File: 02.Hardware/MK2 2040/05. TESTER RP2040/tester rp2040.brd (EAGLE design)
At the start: 135 x 56 mm, 59 parts, among them IC1 MAX4634EUB+T, J1 302-S201, Q1 PJA3416AE_R1_00001, Q2 2N7002PW, Q3 2N7002PW, Q4 RQ3G110ATTB, Q5 PJA3416AE_R1_00001, Q6 2N7002PW, Q7 RQ3G110ATTB, Q8 PJA3416AE_R1_00001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

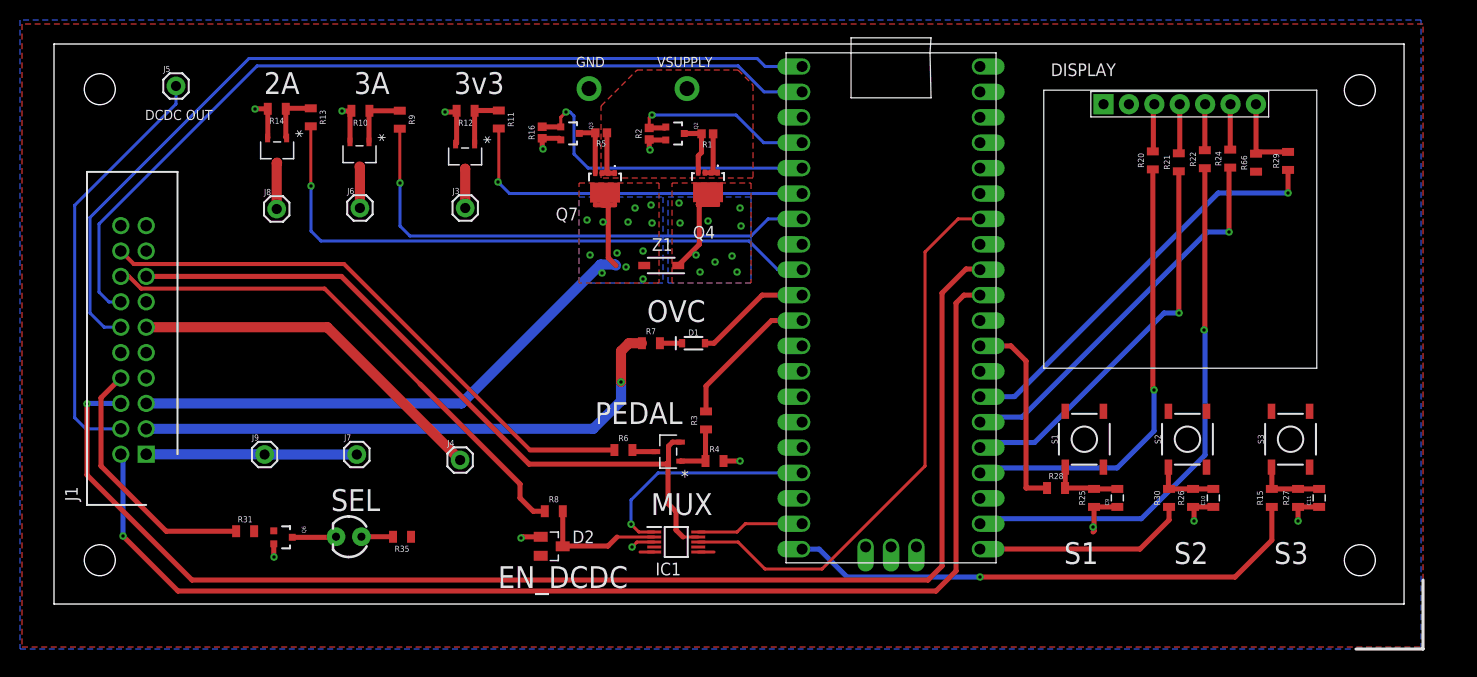
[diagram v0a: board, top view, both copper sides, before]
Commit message: Fix errors.
Cooper clereance 6mil ->8mil.
Isolate de los planos a 0,254 mils.
DRC aproved
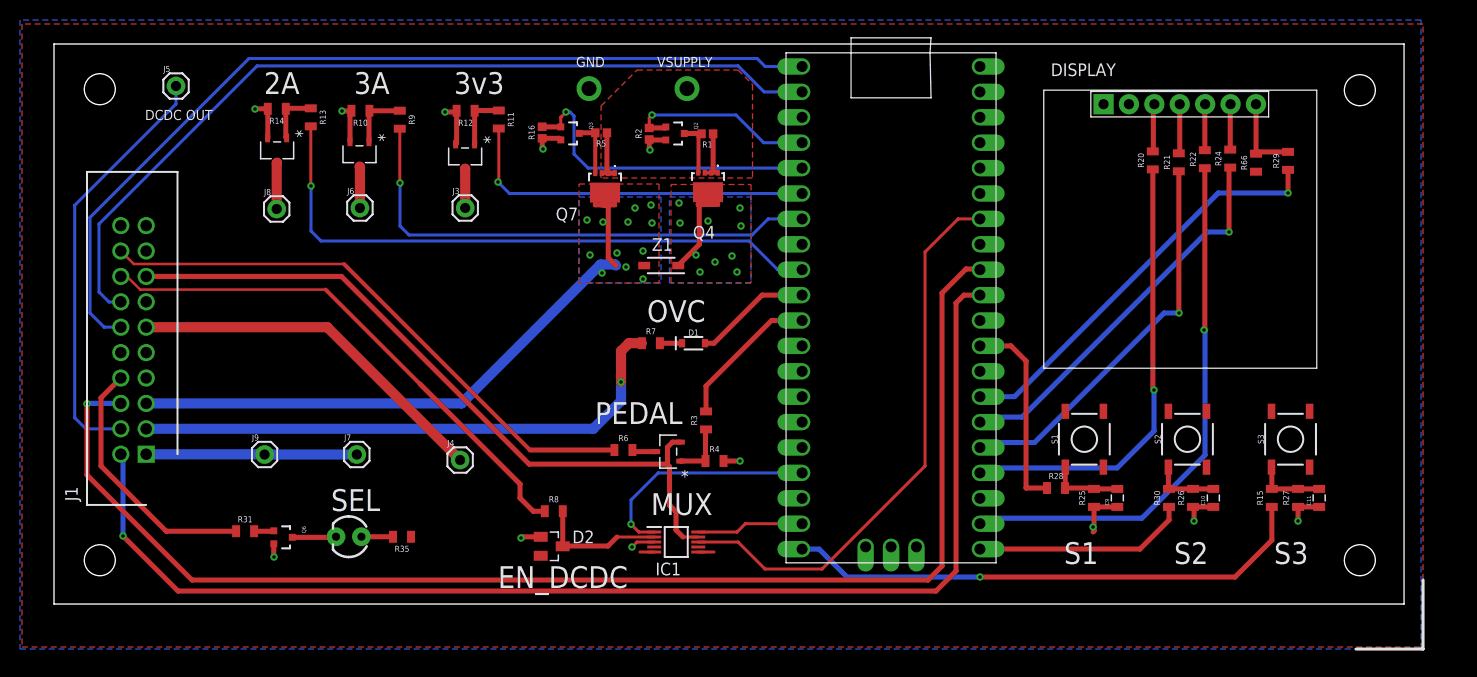
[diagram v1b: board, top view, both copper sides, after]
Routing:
- net N$24: track 0.00 -> 1.98 mm
- net PEDAL-: track 73.2 -> 72.6 mm

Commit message: Revision de PCB (DGB)
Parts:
- R15, R28, R30: value (none) -> 100R
- R25, R26, R27: value (none) -> 2k2
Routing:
- net EN_TPS54531: track 52.9 -> 79.8 mm, vias 0 -> 2
- net PEDAL+: track 57.6 -> 68.7 mm
- net DSP_RST: track 54.1 -> 55.3 mm
- net N$59: track 56.0 -> 54.9 mm
- net 3V3: track 3.00 -> 3.58 mm

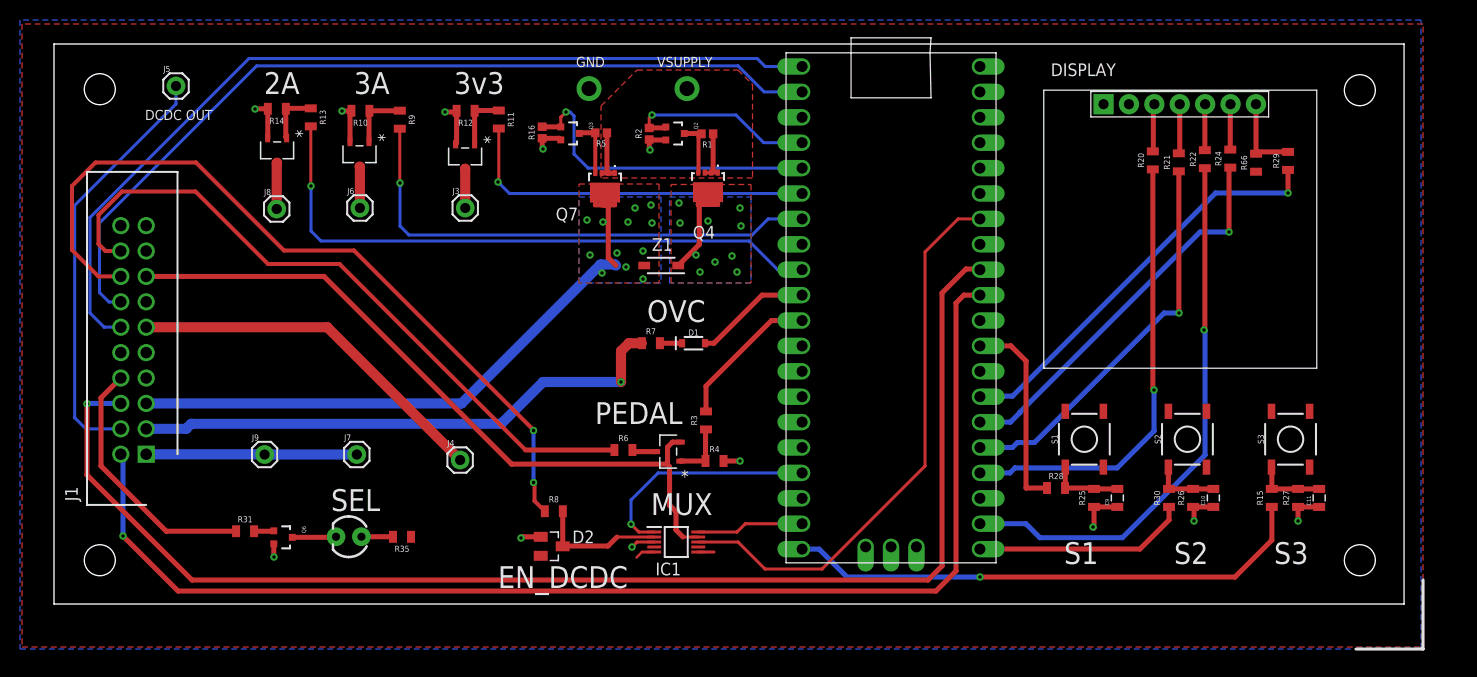
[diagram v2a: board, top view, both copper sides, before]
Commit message: Correccion Errores
Señal Vcc sin conectar.
Añadido sensado de señales VBUS_SENSE y OVC_ALARM.
Mejorado el Plano de GND para evitar estrangulamientos.
Ensanchadas las pistas que conectan con vias.
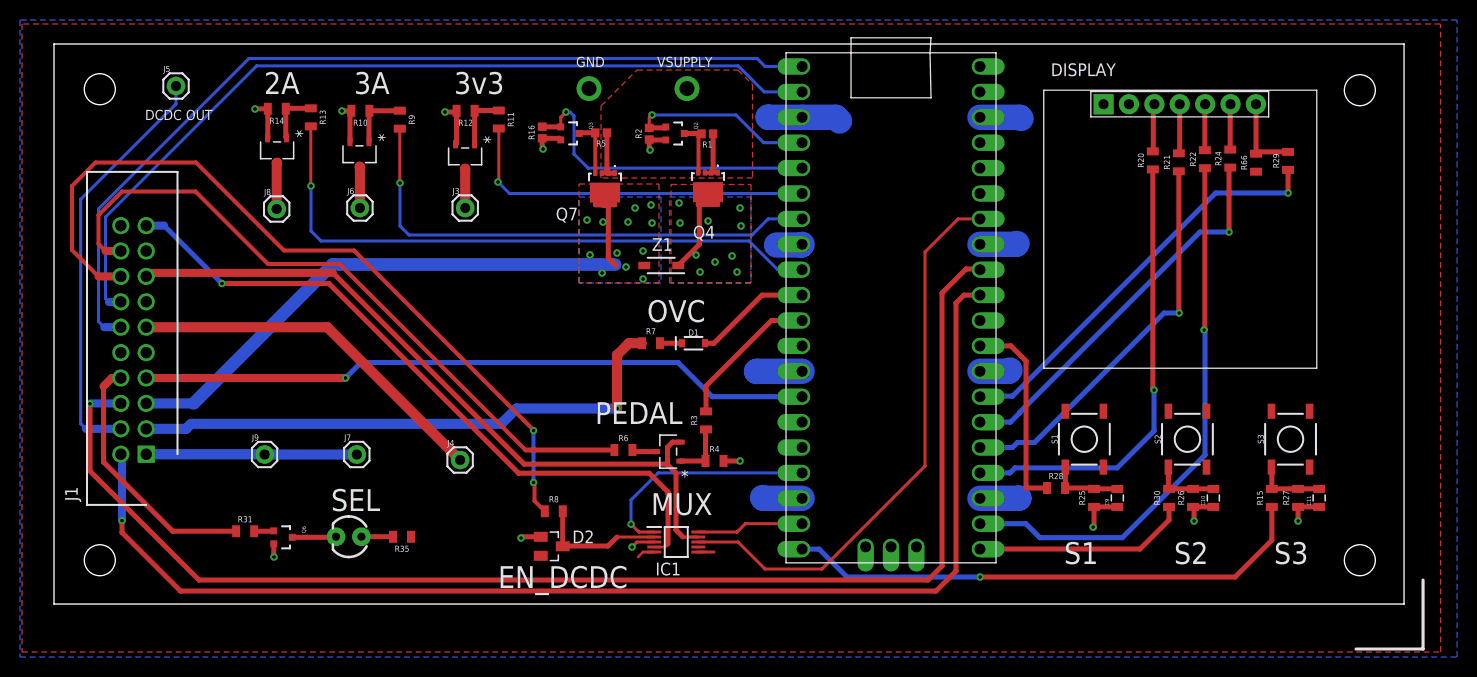
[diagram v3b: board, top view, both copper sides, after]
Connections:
- removed net N$37: X1.GP10
- removed net N$53: IC1.4
- removed net VCC: R66.1
- net 3V3: now also R66.1
- net OVC_ALARM: now also X1.GP10
- net VBUS_SENSE: now also IC1.4
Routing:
- net VBUS_SENSE: track 0.00 -> 69.9 mm, vias 0 -> 1
- net OVC_ALARM: track 0.00 -> 67.6 mm, vias 0 -> 1
- net GND: track 37.7 -> 71.1 mm
- net N$59: track 54.9 -> 56.2 mm
- net ISENSE: track 133.1 -> 132.3 mm
- net USB_D+: track 91.3 -> 90.6 mm
- net EN_TPS54531: track 79.8 -> 79.2 mm

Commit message: Cambio de R7
El valor se cambia para tener en cuenta la R1 presente en la tarjeta cuando la señal OVC_ALARM es activada y prevenir la raspi de una subida de tension en la entrada digital.
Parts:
- R7: value 51k -> 10k
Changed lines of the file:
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@@
 <attribute name="VALUE" x="78.94" y="22.511" size="0.6096" layer="27" font="vector" ratio="20" align="top-center"/>
 </element>
-<element name="R7" library="SparkFun-Resistors" library_urn="urn:adsk.eagle:library:532" package="0805" package3d_urn="urn:adsk.eagle:package:39651/1" value="51k" x="81.69" y="34.08" smashed="yes">
+<element name="R7" library="SparkFun-Resistors" library_urn="urn:adsk.eagle:library:532" package="0805" package3d_urn="urn:adsk.eagle:package:39651/1" value="10k" x="81.69" y="34.08" smashed="yes">
 <attribute name="NAME" x="81.69" y="34.969" size="0.6096" layer="25" font="vector" ratio="20" align="bottom-center"/>
 <attribute name="PROD_ID" value=" " x="96.93" y="-82.76" size="1.778" layer="27" display="off"/>
